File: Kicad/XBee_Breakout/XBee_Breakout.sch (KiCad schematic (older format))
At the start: 7 parts, among them J1 Conn_01x02, J2 Conn_01x04, U1 XBEE

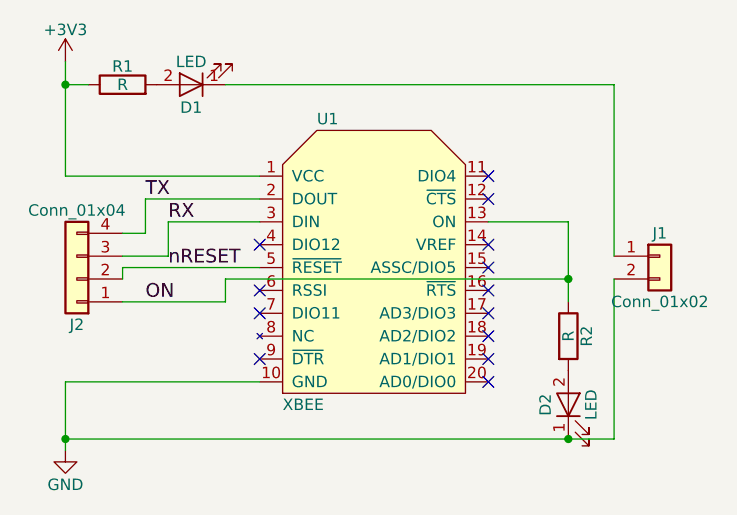
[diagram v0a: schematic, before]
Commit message: Corrected 3V3 bug!
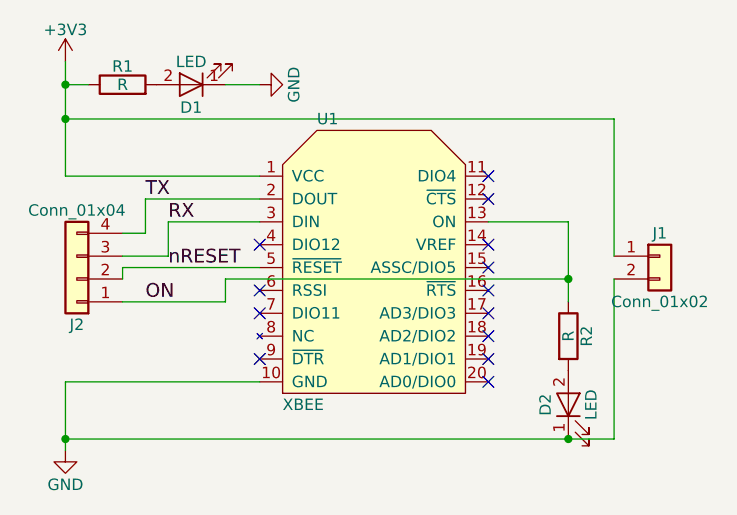
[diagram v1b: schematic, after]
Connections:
- net +3V3: now also J1.1 (Pin_1)
- net GND: now also D1.1 (K)
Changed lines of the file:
@@
 	2800 2300 2700 2300
 Connection ~ 2700 2300
-Wire Wire Line
-	5100 2300 3400 2300
 Connection ~ 4900 3850
 Wire Wire Line
@@
 	5100 3850 5100 3150
 Wire Wire Line
-	5100 3050 5100 2300
+	5100 3050 5100 2450
 Text Label 3050 2800 0    60   ~ 0
 TX
@@
 Wire Wire Line
 	3550 3600 2700 3600
+Wire Wire Line
+	5100 2450 2700 2450
+Connection ~ 2700 2450
+$Comp
+L GND #PWR?
+U 1 1 5A0CEF92
+P 3550 2300
+F 0 "#PWR?" H 3550 2050 50  0001 C CNN
+F 1 "GND" H 3550 2150 50  0000 C CNN
+F 2 "" H 3550 2300 50  0001 C CNN
+F 3 "" H 3550 2300 50  0001 C CNN
+	1    3550 2300
+	0    -1   -1   0
+$EndComp
+Wire Wire Line
+	3400 2300 3550 2300
 $EndSCHEMATC
